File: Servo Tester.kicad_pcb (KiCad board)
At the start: 2 copper layers, 10 parts, among them J1 Conn_01x02_Pin, J2 Conn_01x03_Pin, U1 NE555P

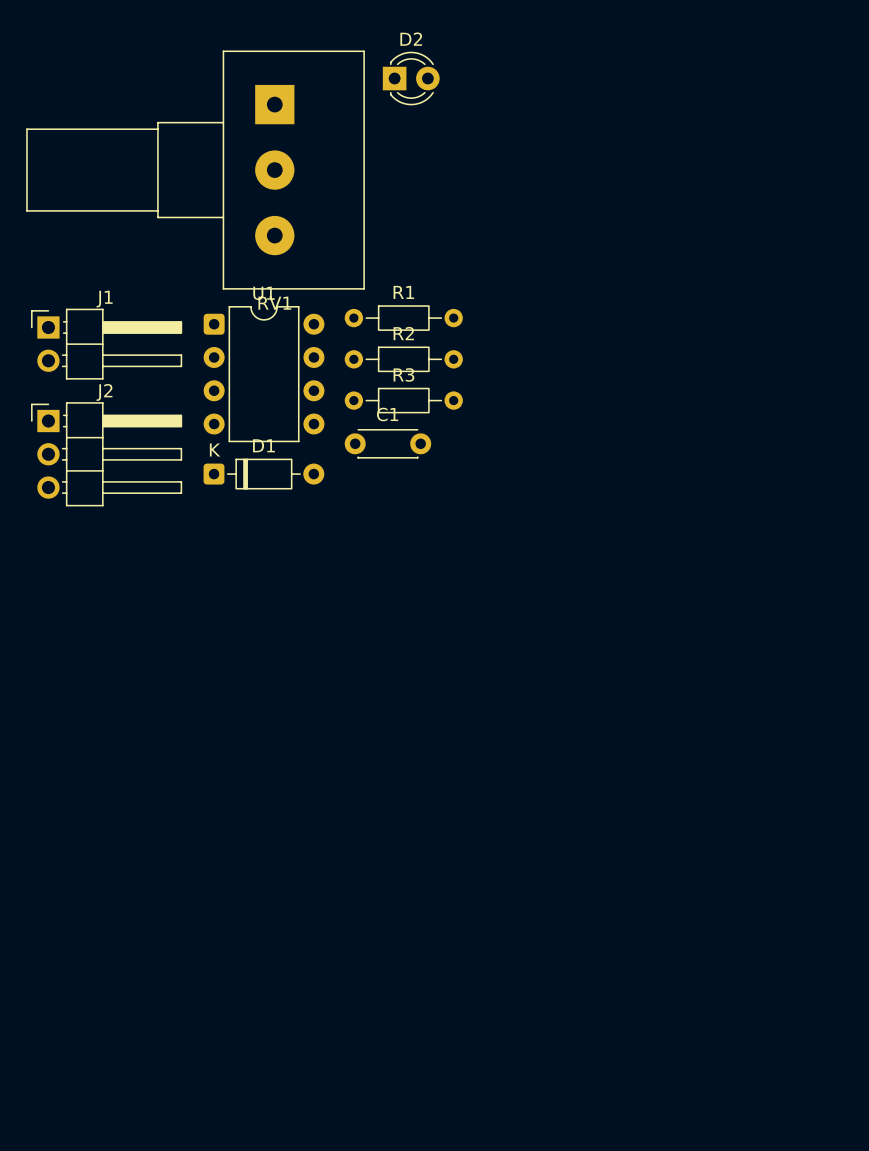
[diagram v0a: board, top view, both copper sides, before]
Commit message: Placed Footprints at Desired location in PCB
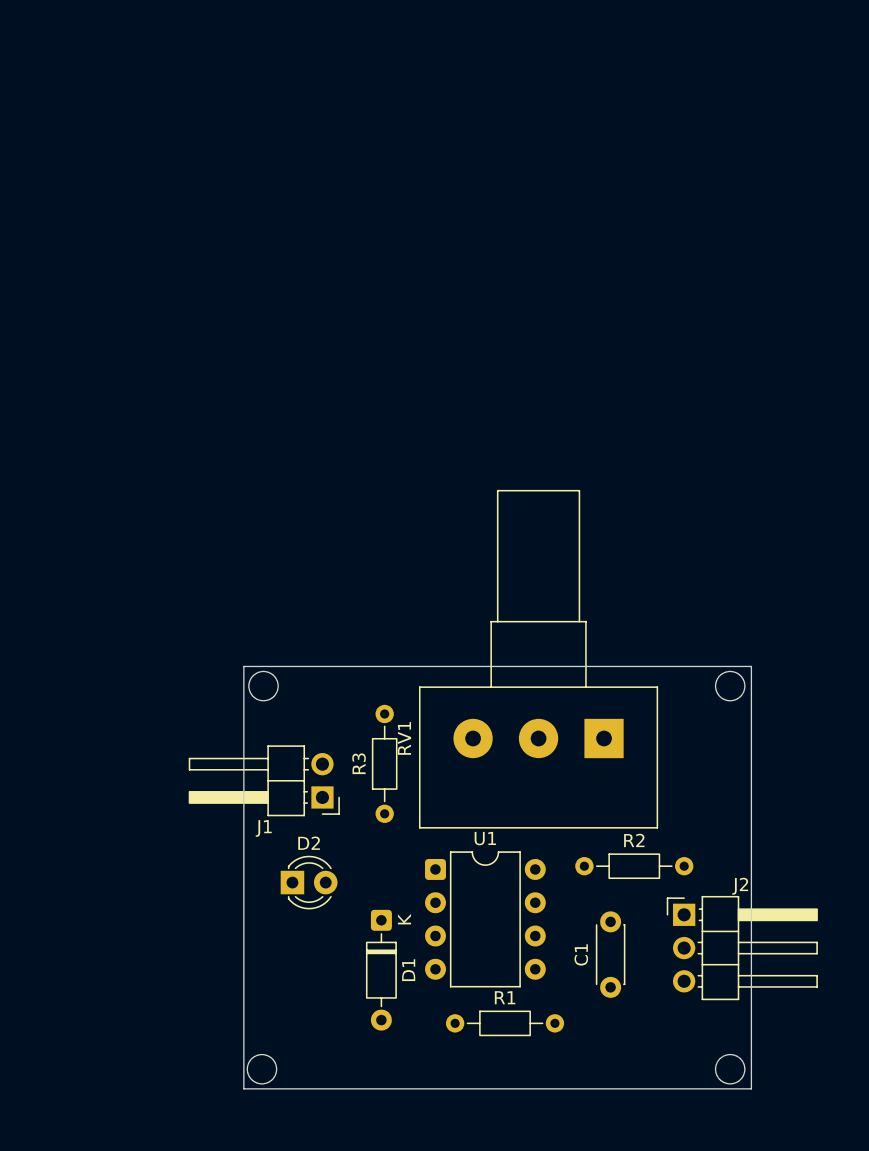
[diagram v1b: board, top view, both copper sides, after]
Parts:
- moved D2 61.9 mm to (131.2, 101.5)
- moved J2 61.5 mm to (161.1, 104.0)
- moved RV1 54.5 mm to (155.0, 90.5), turned to -90 degrees
- moved R1 54.4 mm to (143.6, 112.2)
- moved C1 45.9 mm to (155.5, 109.5), turned to 90 degrees
- moved U1 44.9 mm to (142.1, 100.5)
- moved R2 42.5 mm to (153.5, 100.2)
- moved J1 41.5 mm to (133.5, 95.0), turned to 180 degrees
- moved D1 36.4 mm to (138.0, 104.4), turned to -90 degrees
- moved R3 31.6 mm to (138.2, 96.2), turned to 90 degrees
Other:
- board outline added: 38.8 x 32.2 mm

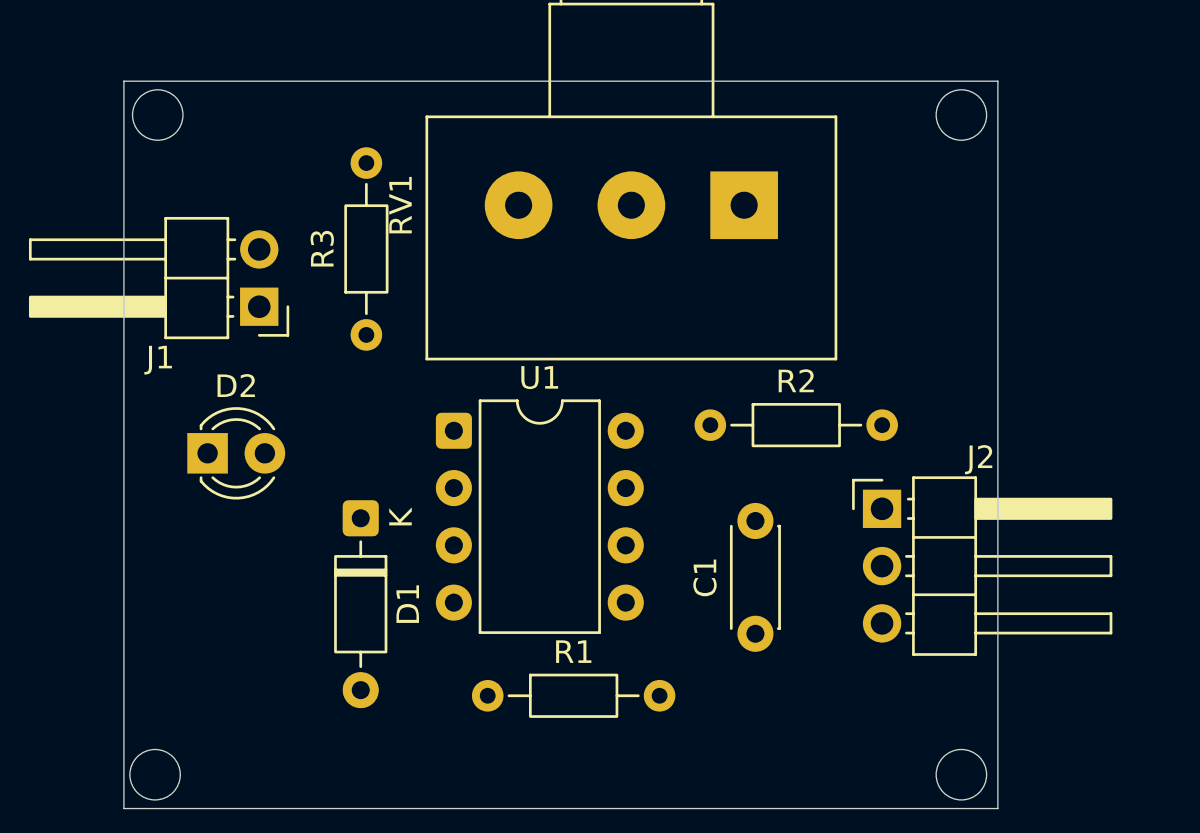
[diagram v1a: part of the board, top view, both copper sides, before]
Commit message: PCB layout with Tracks
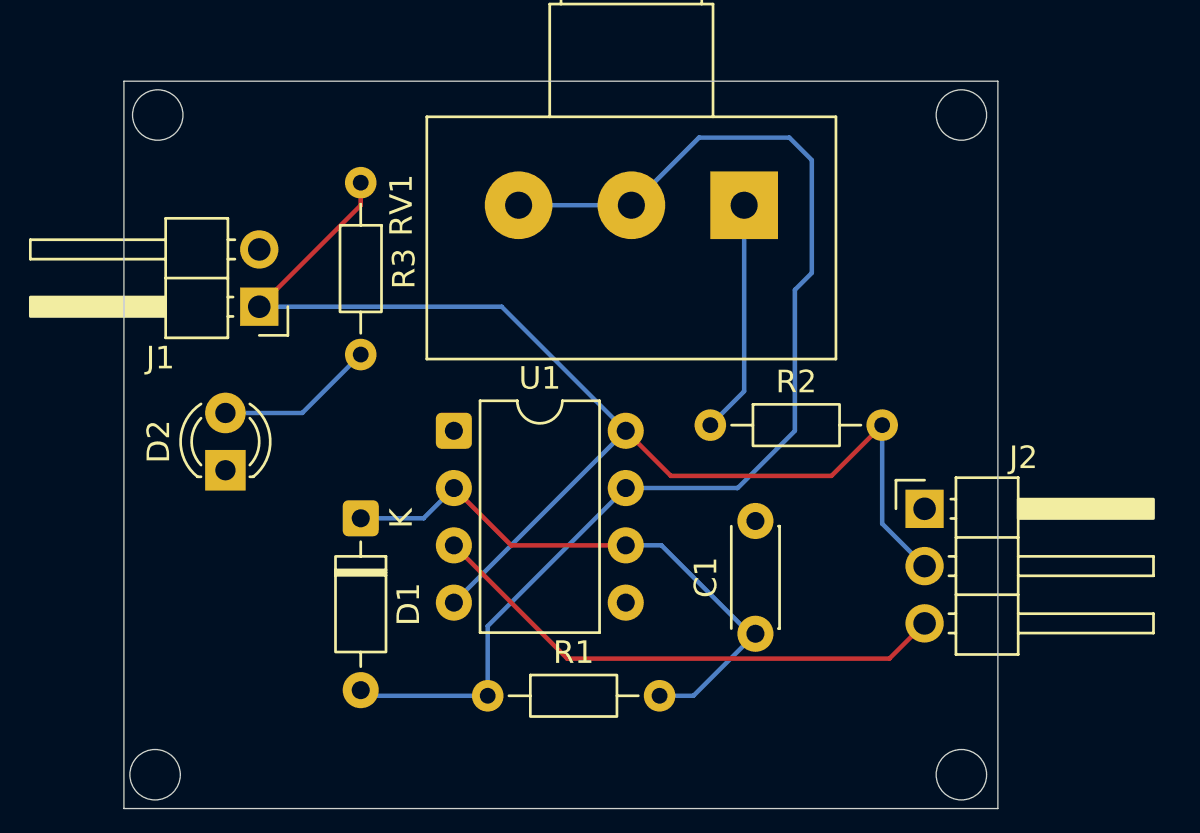
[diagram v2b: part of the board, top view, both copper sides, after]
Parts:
- moved R3 6.75 mm to (138.0, 89.5), turned to -90 degrees
- moved J2 1.88 mm to (163.0, 104.0)
- moved D2 1.09 mm to (132.0, 102.2), turned to 90 degrees
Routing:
- net Net-(J1-Pin_1): track 0.00 -> 56.8 mm
- net Net-(D1-A): track 0.00 -> 53.0 mm
- net Net-(D1-K): track 0.00 -> 26.1 mm
- net Net-(J2-Pin_3): track 0.00 -> 23.6 mm
- net Net-(R2-Pad1): track 0.00 -> 10.4 mm
- net Net-(D2-A): track 0.00 -> 7.07 mm

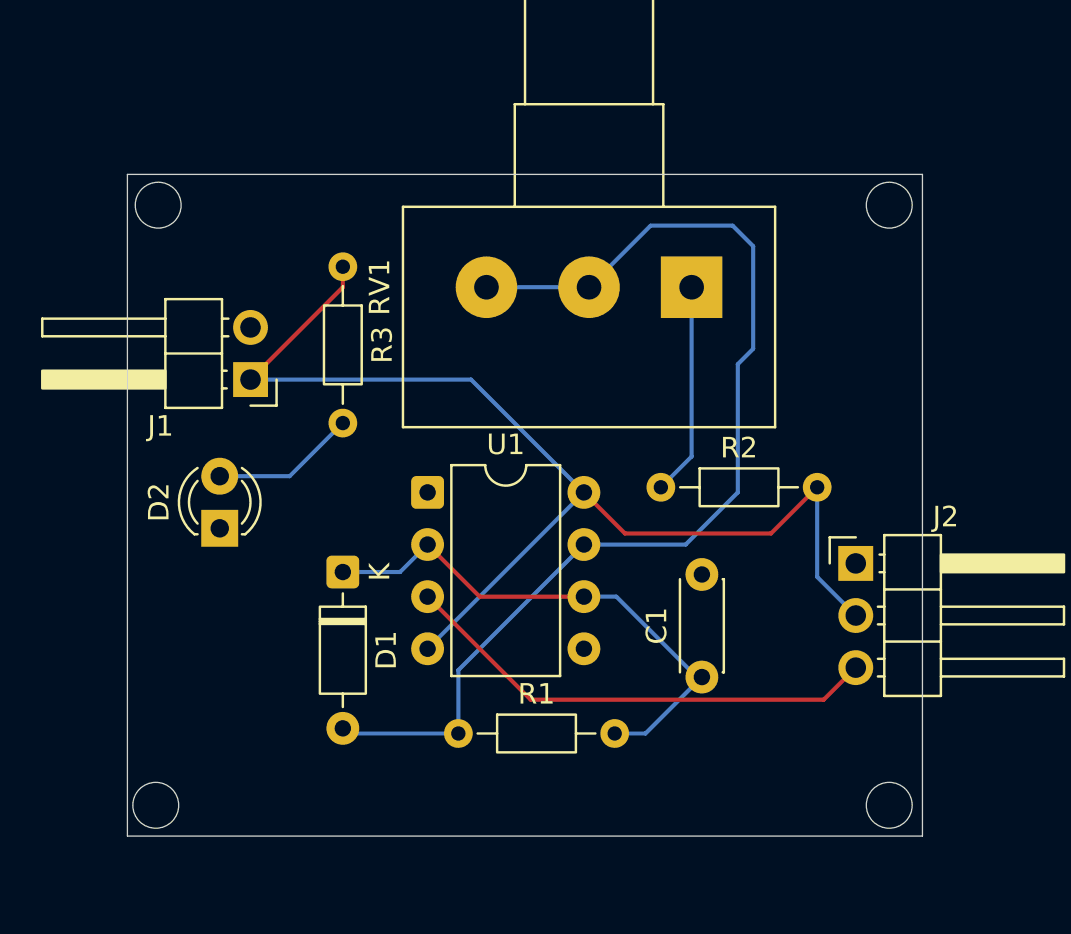
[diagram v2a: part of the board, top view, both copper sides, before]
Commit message: PCB layout with Copper Field Zone GND added
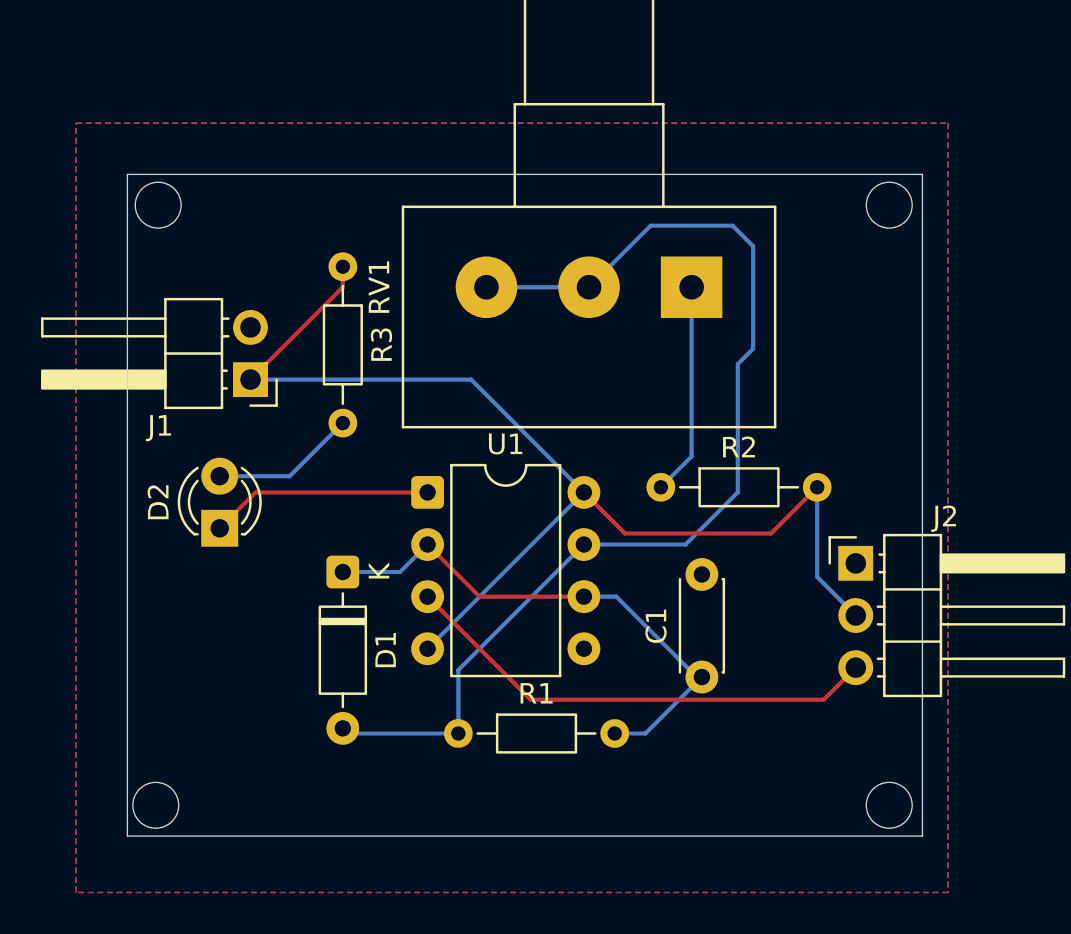
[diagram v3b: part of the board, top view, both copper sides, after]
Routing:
- net GND: track 0.00 -> 10.9 mm
- added copper zone on B.Cu, net GND
- added copper zone on F.Cu, net GND
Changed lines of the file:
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@@
+	)
+	(segment
+		(start 142.13 100.5)
+		(end 133.75 100.5)
+		(width 0.2)
+		(layer "F.Cu")
+		(net 2)
+	)
+	(segment
+		(start 133.75 100.5)
+		(end 132 102.25)
+		(width 0.2)
+		(layer "F.Cu")
+		(net 2)
 	)
 	(segment
@@
 		(net 7)
 	)
+	(zone
+		(net 2)
+		(net_name "GND")
+		(layers "F.Cu" "B.Cu")
+		(hatch edge 0.5)
+		(connect_pads
+			(clearance 0.5)
+		)
+		(min_thickness 0.25)
+		(filled_areas_thickness no)
+		(fill yes
+			(thermal_gap 0.5)
+			(thermal_bridge_width 0.5)
+		)
+		(polygon
+			(pts
+				(xy 125 82.5) (xy 167.5 82.5) (xy 167.5 120) (xy 125 120)
+			)
+		)
+	)
 	(embedded_fonts no)
